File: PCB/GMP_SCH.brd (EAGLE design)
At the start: 24 parts, among them CN1 1X4-3.5MM, CN2 1X4-3.5MM, IC1 MS560702BA03-50, Q1 TSM200N03DPQ33_RGG

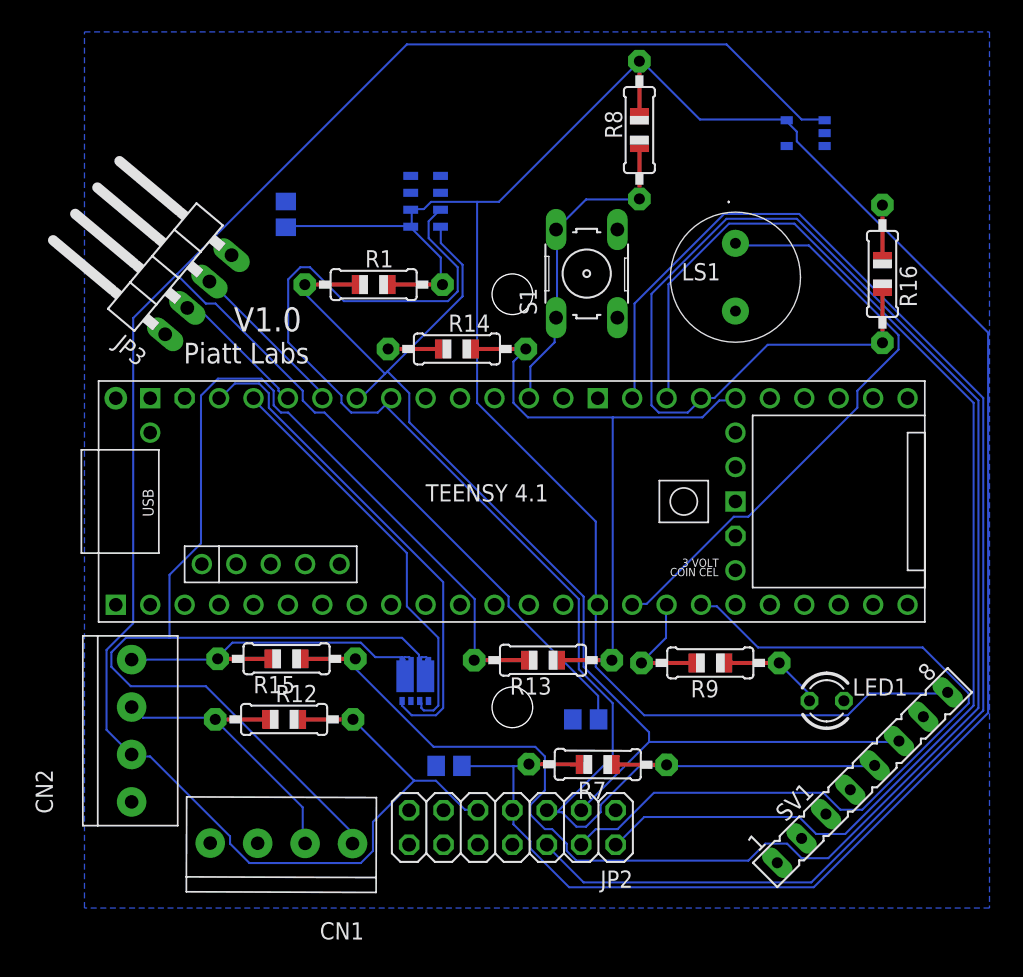
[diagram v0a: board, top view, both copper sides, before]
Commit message: rerouted the main board. one pin pending
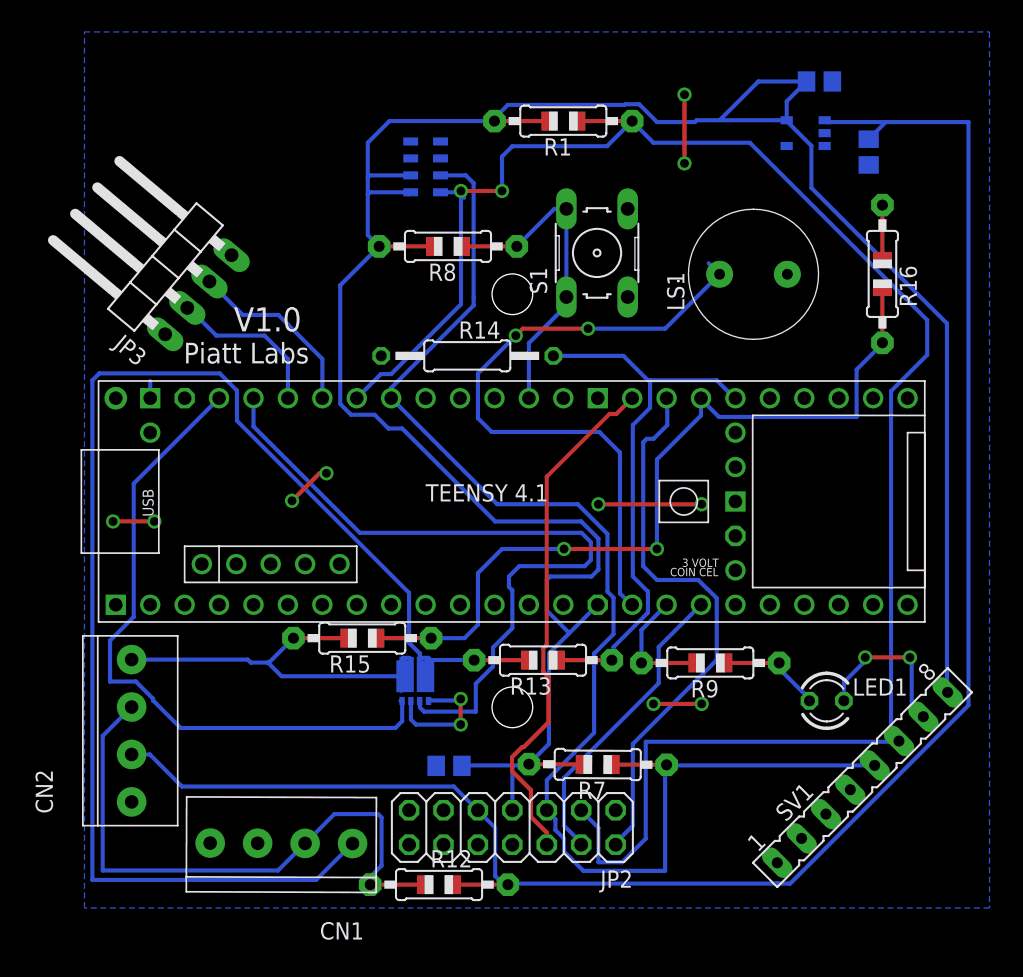
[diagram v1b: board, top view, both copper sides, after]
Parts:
- R14: device adafruit:0805-THM -> rcl:0207/12
- moved C4 46.8 mm to (56.8, 56.2), turned to 270 degrees
- moved C1 40.6 mm to (53.1, 61.4), turned to 180 degrees
- moved R1 18.5 mm to (34.2, 58.5), turned to 180 degrees
- moved R12 16.7 mm to (25.1, 2.16)
- moved R8 16.5 mm to (25.7, 49.3), turned to 180 degrees
- moved R15 5.79 mm to (19.4, 20.3)
- moved LS1 2.57 mm to (45.8, 47.2), turned to 90 degrees
- moved IC1 2.54 mm to (24.1, 55.1)
- moved S1 1.70 mm to (36.7, 48.8)
- moved R14 0.92 mm to (27.2, 41.2)
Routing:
- net SENSE_2: track 144.8 -> 52.4 mm, vias 0 -> 2
- net SPI_MISO: track 102.9 -> 38.8 mm
- net V_BAT: track 182.3 -> 129.0 mm
- net SPI_CS: track 92.4 -> 41.3 mm
- net GND: track 0.00 -> 45.6 mm, vias 0 -> 14
- net I2C_SCL: track 86.8 -> 132.4 mm, vias 0 -> 2
- net V_3.3: track 218.0 -> 175.1 mm
- net SPI_MOSI: track 57.2 -> 22.4 mm
- net EMATCH_1: track 30.4 -> 54.3 mm
- net EMATCH_N+: track 18.4 -> 41.7 mm
- net EMATCH_2: track 36.9 -> 49.1 mm
- net I2C_SDA: track 103.8 -> 98.7 mm
- net N$15: track 44.1 -> 48.7 mm, vias 0 -> 2
- net EMATCH_2-: track 23.2 -> 26.7 mm
- net EMATCH_1-: track 102.2 -> 99.4 mm
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
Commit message: fix file issues
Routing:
- net V_BAT: track 129.0 -> 131.5 mm
- net V_3.3: track 175.1 -> 175.9 mm
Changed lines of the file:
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@@
 <layer number="19" name="Unrouted" color="6" fill="1" visible="yes" active="yes"/>
 <layer number="20" name="Dimension" color="24" fill="1" visible="yes" active="yes"/>
-<layer number="21" name="tPlace" color="7" fill="1" visible="yes" active="yes"/>
+<layer number="21" name="tPlace" color="7" fill="1" visible="no" active="yes"/>
 <layer number="22" name="bPlace" color="7" fill="1" visible="yes" active="yes"/>
-<layer number="23" name="tOrigins" color="15" fill="1" visible="yes" active="yes"/>
+<layer number="23" name="tOrigins" color="15" fill="1" visible="no" active="yes"/>
 <layer number="24" name="bOrigins" color="15" fill="1" visible="yes" active="yes"/>
-<layer number="25" name="tNames" color="7" fill="1" visible="yes" active="yes"/>
+<layer number="25" name="tNames" color="7" fill="1" visible="no" active="yes"/>
 <layer number="26" name="bNames" color="7" fill="1" visible="yes" active="yes"/>
 <layer number="27" name="tValues" color="7" fill="1" visible="no" active="yes"/>
@@
 <layer number="37" name="tTest" color="7" fill="1" visible="no" active="yes"/>
 <layer number="38" name="bTest" color="7" fill="1" visible="no" active="yes"/>
-<layer number="39" name="tKeepout" color="4" fill="11" visible="yes" active="yes"/>
+<layer number="39" name="tKeepout" color="4" fill="11" visible="no" active="yes"/>
 <layer number="40" name="bKeepout" color="1" fill="11" visible="yes" active="yes"/>
-<layer number="41" name="tRestrict" color="4" fill="10" visible="yes" active="yes"/>
+<layer number="41" name="tRestrict" color="4" fill="10" visible="no" active="yes"/>
 <layer number="42" name="bRestrict" color="1" fill="10" visible="yes" active="yes"/>
 <layer number="43" name="vRestrict" color="2" fill="10" visible="no" active="yes"/>
@@
 <layer number="49" name="Reference" color="7" fill="1" visible="no" active="yes"/>
 <layer number="50" name="dxf" color="7" fill="1" visible="no" active="no"/>
-<layer number="51" name="tDocu" color="7" fill="1" visible="yes" active="yes"/>
+<layer number="51" name="tDocu" color="7" fill="1" visible="no" active="yes"/>
 <layer number="52" name="bDocu" color="7" fill="1" visible="yes" active="yes"/>
 <layer number="53" name="tGND_GNDA" color="7" fill="9" visible="no" active="no"/>
@@
 <wire x1="14.224" y1="30.48" x2="16.256" y2="32.512" width="0.3048" layer="1"/>
 <wire x1="16.256" y1="32.512" x2="16.764" y2="32.512" width="0.3048" layer="1"/>
-<wire x1="36.83" y1="30.226" x2="36.7792" y2="38.0492" width="0" layer="19" extent="1-1"/>
 </signal>
 <signal name="V_BAT">
@@
 <contactref element="CN2" pad="3"/>
 <contactref element="R12" pad="2"/>
-<wire x1="64.135" y1="58.42" x2="58.0288" y2="58.42" width="0.3048" layer="16"/>
+<wire x1="64.643" y1="58.42" x2="58.0288" y2="58.42" width="0.3048" layer="16"/>
 <wire x1="58.0288" y1="58.42" x2="53.6575" y2="58.42" width="0.3048" layer="16"/>
-<wire x1="64.135" y1="15.39875" x2="64.135" y2="58.42" width="0.3048" layer="16"/>
-<wire x1="50.95875" y1="2.2225" x2="64.135" y2="15.39875" width="0.3048" layer="16"/>
-<wire x1="27.94" y1="7.62" x2="28.194" y2="7.366" width="0.3048" layer="16"/>
-<wire x1="28.194" y1="7.366" x2="29.21" y2="6.35" width="0.3048" layer="16"/>
+<wire x1="64.643" y1="14.12875" x2="64.643" y2="58.42" width="0.3048" layer="16"/>
+<wire x1="51.84775" y1="1.3335" x2="64.643" y2="14.12875" width="0.3048" layer="16"/>
+<wire x1="27.94" y1="7.62" x2="29.21" y2="6.35" width="0.3048" layer="16"/>
 <wire x1="53.6575" y1="58.42" x2="53.5208" y2="58.5572" width="0.3048" layer="16"/>
 <wire x1="27.94" y1="7.62" x2="27.94" y2="7.6454" width="0.3048" layer="16"/>
@@
 <wire x1="29.21" y1="2.794" x2="29.845" y2="2.159" width="0.3048" layer="16"/>
 <wire x1="50.00315625" y1="2.286" x2="50.0507125" y2="2.23844375" width="0.3048" layer="16"/>
-<wire x1="50.94280625" y1="2.23844375" x2="50.95875" y2="2.2225" width="0.3048" layer="16"/>
+<wire x1="50.94280625" y1="2.23844375" x2="51.84775" y2="1.3335" width="0.3048" layer="16"/>
 <wire x1="50.94280625" y1="2.23844375" x2="50.0507125" y2="2.23844375" width="0.3048" layer="16"/>
 <wire x1="30.1498" y1="2.159" x2="29.845" y2="2.159" width="0.3048" layer="16"/>
@@
 <contactref element="SV1" pad="8"/>
 <wire x1="52.54625" y1="56.67375" x2="50.8" y2="58.42" width="0.3048" layer="16"/>
-<wire x1="52.54625" y1="53.56225" x2="52.54625" y2="56.67375" width="0.3048" layer="16"/>
-<wire x1="62.5475" y1="43.561" x2="52.54625" y2="53.56225" width="0.3048" layer="16"/>
-<wire x1="62.5475" y1="16.35125" x2="62.5475" y2="43.561" width="0.3048" layer="16"/>
+<wire x1="52.54625" y1="54.83225" x2="52.54625" y2="56.67375" width="0.3048" layer="16"/>
+<wire x1="63.5635" y1="43.815" x2="52.54625" y2="54.83225" width="0.3048" layer="16"/>
+<wire x1="62.597978125" y1="16.344578125" x2="63.5635" y2="17.3101" width="0.3048" layer="16"/>
+<wire x1="63.5635" y1="43.815" x2="63.5635" y2="17.3101" width="0.3048" layer="16"/>
 <wire x1="50.8" y1="58.42" x2="50.7208" y2="58.5572" width="0.3048" layer="16"/>
-<wire x1="62.5475" y1="16.35125" x2="62.597978125" y2="16.344578125" width="0.3048" layer="16"/>
 <wire x1="23.01875" y1="53.18125" x2="22.9792" y2="53.243" width="0.3048" layer="16"/>
 <wire x1="31.59125" y1="10.95375" x2="30.48" y2="10.95375" width="0.3048" layer="16"/>
@@
 <wire x1="23.97125" y1="14.9225" x2="23.65375" y2="15.24" width="0.3048" layer="16"/>
 <wire x1="27.78125" y1="14.9225" x2="23.97125" y2="14.9225" width="0.3048" layer="16"/>
-<wire x1="27.78125" y1="16.98625" x2="27.78125" y2="14.9225" width="0.3048" layer="16"/>
-<wire x1="27.78125" y1="16.98625" x2="29.05125" y2="18.25625" width="0.3048" layer="16"/>
+<wire x1="27.78125" y1="16.47825" x2="27.78125" y2="14.9225" width="0.3048" layer="16"/>
+<wire x1="27.78125" y1="16.47825" x2="30.06725" y2="18.76425" width="0.3048" layer="16"/>
 <wire x1="11.3792" y1="35.96005" x2="19.224625" y2="28.114625" width="0.3048" layer="16"/>
 <wire x1="23.65375" y1="15.5575" x2="23.6422" y2="15.709" width="0.3048" layer="16"/>
 <wire x1="11.3792" y1="35.96005" x2="11.3792" y2="38.0492" width="0.3048" layer="16"/>
-<wire x1="29.05125" y1="19.65325" x2="30.48" y2="21.082" width="0.3048" layer="16"/>
+<wire x1="30.06725" y1="20.66925" x2="30.48" y2="21.082" width="0.3048" layer="16"/>
 <wire x1="30.48" y1="21.082" x2="30.48" y2="23.876" width="0.3048" layer="16"/>
 <wire x1="30.48" y1="23.876" x2="30.226" y2="24.13" width="0.3048" layer="16"/>
@@
 <wire x1="36.2712" y1="27.432" x2="35.588575" y2="28.114625" width="0.3048" layer="16"/>
 <wire x1="35.588575" y1="28.114625" x2="19.224625" y2="28.114625" width="0.3048" layer="16"/>
-<wire x1="29.05125" y1="18.25625" x2="29.05125" y2="19.65325" width="0.3048" layer="16"/>
+<wire x1="30.06725" y1="18.76425" x2="30.06725" y2="20.66925" width="0.3048" layer="16"/>
 <wire x1="30.226" y1="24.892" x2="30.988" y2="25.654" width="0.3048" layer="16"/>
 </signal>

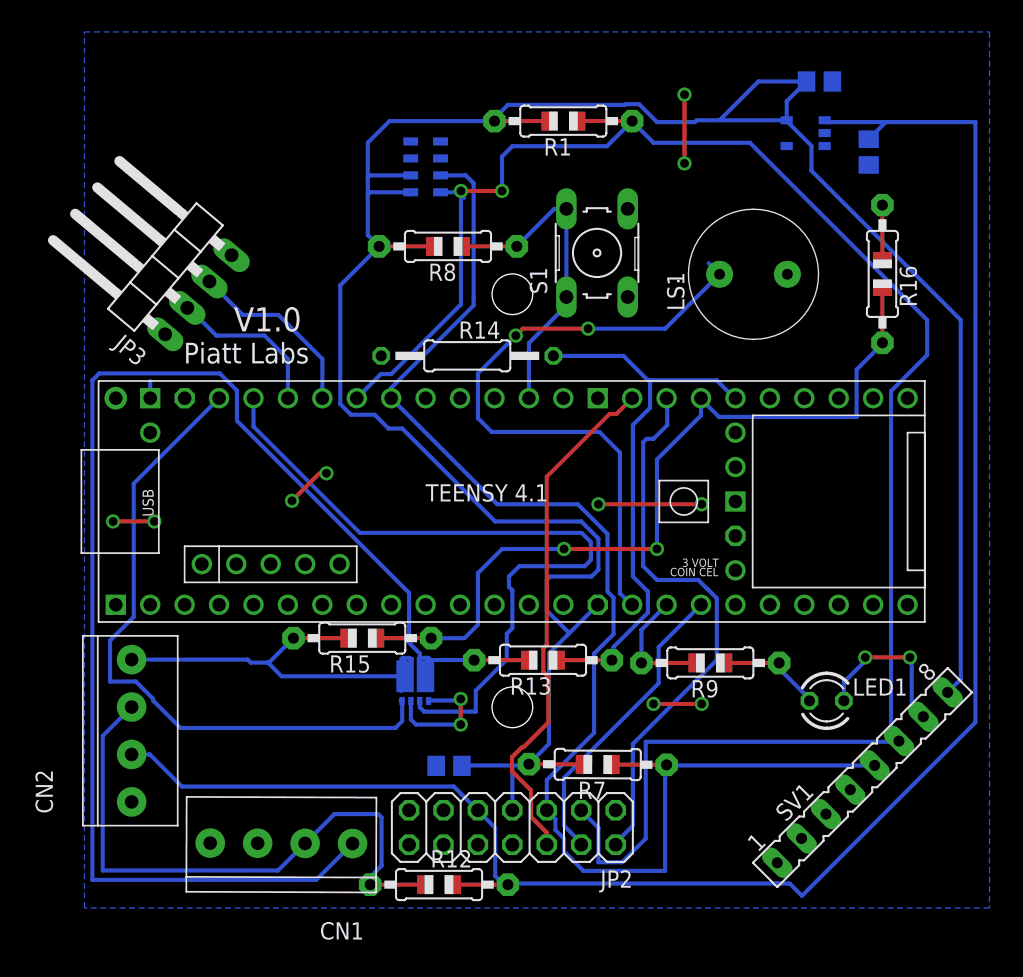
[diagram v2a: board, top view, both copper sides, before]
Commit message: Add files via upload
Fixed silly little airwire due to decals
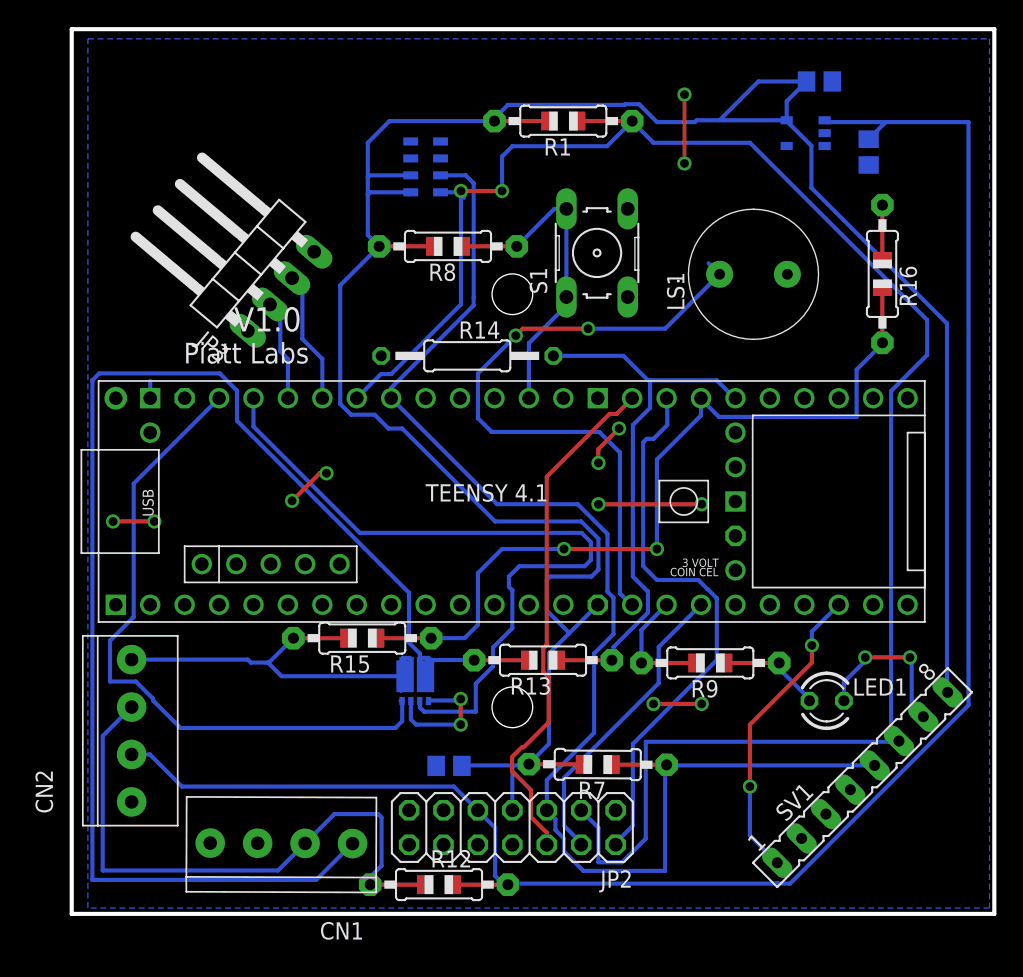
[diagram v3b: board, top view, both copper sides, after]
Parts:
- moved JP3 6.10 mm to (10.5, 48.4)
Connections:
- net INT: now also U$1.30-CRX3; no longer U$1.17-A3/TX4/SDA1
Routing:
- net INT: track 0.00 -> 22.6 mm, vias 0 -> 2
- net SERIAL_ESP_RX: track 11.9 -> 7.47 mm
- net SERIAL_ESP_TX: track 13.6 -> 9.79 mm
- net GND: track 45.6 -> 48.8 mm, vias 14 -> 16
- net V_BAT: track 131.5 -> 129.0 mm
- net V_3.3: track 175.9 -> 175.1 mm
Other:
- board outline added: 68.1 x 65.3 mm
- board text added: "Matthew 10:28"
- board text added: "Not because it is easy but because it is hard"
- board text added: "V1.2"
